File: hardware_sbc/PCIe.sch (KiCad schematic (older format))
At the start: 21 parts, among them J5 Bus_PCI_Express_Mini, U1 IMX8MM

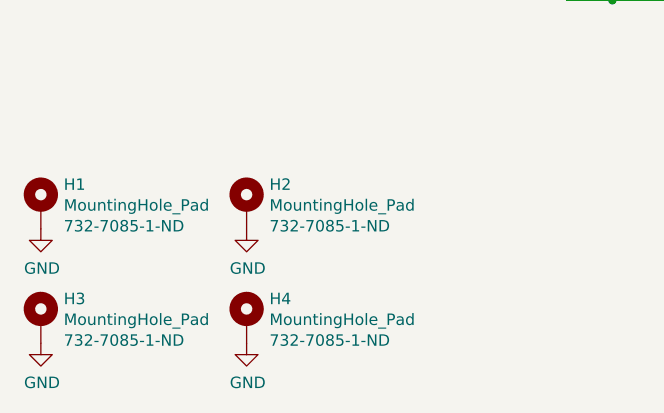
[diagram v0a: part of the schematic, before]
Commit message: BOM and misc fixes for production of 0.9 boards
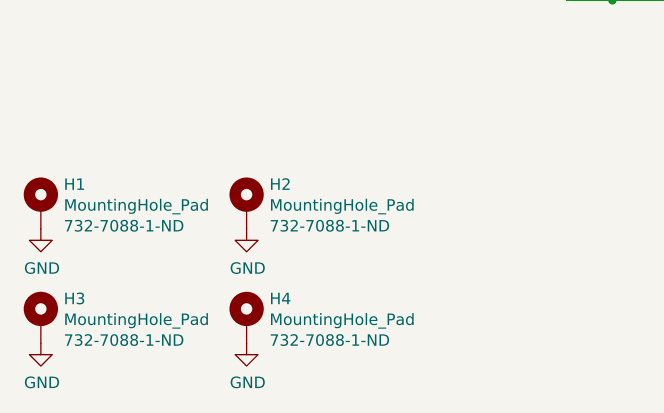
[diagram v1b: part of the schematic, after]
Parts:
- C121, C122, C123: Mfgrpart (none) -> GRM033C80J104KE15D; Part GRM033C80J104KE15D -> (none)
- C124, C130: Mfgrpart (none) -> GRM155C80J475MEAAD; Part GRM155C80J475MEAAD -> (none)
- C125, C126, C127: Mfgrpart (none) -> GRM31CR60J227ME11L; Part GRM31CR60J227ME11L -> (none)
- C128, C129: Mfgrpart (none) -> GRM21BC80G476ME15L; Part GRM21BC80G476ME15L -> (none)
- C131: Mfgrpart (none) -> GRM155C80J106ME11D; Part GRM155C80J106ME11D -> (none)
- D2: Mfgrpart (none) -> MM5Z5V1T1G; Part MM5Z5V1T1G -> (none)
- H1, H2, H3, H4: Mfgrpart (none) -> 9774035243R‎; Part 9774030243R -> (none); Vendorpart 732-7085-1-ND -> 732-7088-1-ND‎
- J5: Mfgrpart (none) -> 1775838-2; Part 1775838-2 -> (none)
- R34, R35: Mfgrpart (none) -> RC0201FR-0749R9L; Part RC0201FR-0749R9L -> (none)
- R36: Mfgrpart (none) -> RC0201FR-078K2L; Part RC0201FR-078K2L -> (none)
- U1: Mfgrpart (none) -> MIMX8MM6CVTKZAA; Part MIMX8MM6CVTKZAA -> (none)
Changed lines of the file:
@@
 F 3 "~" H 7200 2600 50  0001 C CNN
 F 4 "TE" H 7350 3750 50  0001 C CNN "Mfgr"
-F 5 "1775838-2" H 7350 3750 50  0001 C CNN "Part"
+F 5 "" H 7350 3750 50  0001 C CNN "Part"
 F 6 "A123340CT-ND" H 7350 3750 50  0001 C CNN "Vendorpart"
+F 7 "1775838-2" H 7350 3750 50  0001 C CNN "Mfgrpart"
 	1    7350 3750
 	1    0    0    1
@@
 F 3 "" H 2950 8900 50  0001 C CNN
 F 4 "NXP" H 3700 6150 50  0001 C CNN "Mfgr"
-F 5 "MIMX8MM6CVTKZAA" H 3700 6150 50  0001 C CNN "Part"
+F 5 "" H 3700 6150 50  0001 C CNN "Part"
 F 6 "568-15276-ND" H 3700 6150 50  0001 C CNN "Vendorpart"
+F 7 "MIMX8MM6CVTKZAA" H 3700 6150 50  0001 C CNN "Mfgrpart"
 	3    3700 6150
 	1    0    0    -1
@@
 F 3 "~" H 5250 4650 50  0001 C CNN
 F 4 "Yageo" H 5250 4650 50  0001 C CNN "Mfgr"
-F 5 "RC0201FR-078K2L" H 5250 4650 50  0001 C CNN "Part"
+F 5 "" H 5250 4650 50  0001 C CNN "Part"
 F 6 "YAG2353CT-ND" H 5250 4650 50  0001 C CNN "Vendorpart"
+F 7 "RC0201FR-078K2L" H 5250 4650 50  0001 C CNN "Mfgrpart"
 	1    5250 4650
 	1    0    0    -1
@@
 F 3 "~" H 5450 3300 50  0001 C CNN
 F 4 "Yageo" H 5450 3300 50  0001 C CNN "Mfgr"
-F 5 "RC0201FR-0749R9L" H 5450 3300 50  0001 C CNN "Part"
+F 5 "" H 5450 3300 50  0001 C CNN "Part"
 F 6 "YAG2702CT-ND" H 5450 3300 50  0001 C CNN "Vendorpart"
+F 7 "RC0201FR-0749R9L" H 5450 3300 50  0001 C CNN "Mfgrpart"
 	1    5450 3300
 	1    0    0    -1
@@
 F 3 "~" H 5850 3300 50  0001 C CNN
 F 4 "Yageo" H 5850 3300 50  0001 C CNN "Mfgr"
-F 5 "RC0201FR-0749R9L" H 5850 3300 50  0001 C CNN "Part"
+F 5 "" H 5850 3300 50  0001 C CNN "Part"
 F 6 "YAG2702CT-ND" H 5850 3300 50  0001 C CNN "Vendorpart"
+F 7 "RC0201FR-0749R9L" H 5850 3300 50  0001 C CNN "Mfgrpart"
 	1    5850 3300
 	1    0    0    -1
@@
 F 3 "~" H 7900 5350 50  0001 C CNN
 F 4 "Murata" H 7900 5350 50  0001 C CNN "Mfgr"
-F 5 "GRM155C80J475MEAAD" H 7900 5350 50  0001 C CNN "Part"
+F 5 "" H 7900 5350 50  0001 C CNN "Part"
 F 6 "490-14458-1-ND" H 7900 5350 50  0001 C CNN "Vendorpart"
+F 7 "GRM155C80J475MEAAD" H 7900 5350 50  0001 C CNN "Mfgrpart"
 	1    7900 5350
 	1    0    0    -1
@@
 F 3 "~" H 8150 5350 50  0001 C CNN
 F 4 "Murata" H 8150 5350 50  0001 C CNN "Mfgr"
-F 5 "GRM155C80J106ME11D" H 8150 5350 50  0001 C CNN "Part"
+F 5 "" H 8150 5350 50  0001 C CNN "Part"
 F 6 "490-13233-1-ND" H 8150 5350 50  0001 C CNN "Vendorpart"
+F 7 "GRM155C80J106ME11D" H 8150 5350 50  0001 C CNN "Mfgrpart"
 	1    8150 5350
 	1    0    0    -1
@@
 F 3 "~" H 6750 5350 50  0001 C CNN
 F 4 "Murata" H 6750 5350 50  0001 C CNN "Mfgr"
-F 5 "GRM21BC80G476ME15L" H 6750 5350 50  0001 C CNN "Part"
+F 5 "" H 6750 5350 50  0001 C CNN "Part"
 F 6 "490-9954-1-ND" H 6750 5350 50  0001 C CNN "Vendorpart"
+F 7 "GRM21BC80G476ME15L" H 6750 5350 50  0001 C CNN "Mfgrpart"
 	1    6750 5350
 	1    0    0    -1
@@
 F 3 "~" H 6500 5350 50  0001 C CNN
 F 4 "Murata" H 6500 5350 50  0001 C CNN "Mfgr"
-F 5 "GRM21BC80G476ME15L" H 6500 5350 50  0001 C CNN "Part"
+F 5 "" H 6500 5350 50  0001 C CNN "Part"
 F 6 "490-9954-1-ND" H 6500 5350 50  0001 C CNN "Vendorpart"
+F 7 "GRM21BC80G476ME15L" H 6500 5350 50  0001 C CNN "Mfgrpart"
 	1    6500 5350
 	1    0    0    -1
@@
 F 3 "~" H 6250 5350 50  0001 C CNN
 F 4 "Murata" H 6250 5350 50  0001 C CNN "Mfgr"
-F 5 "GRM31CR60J227ME11L" H 6250 5350 50  0001 C CNN "Part"
+F 5 "" H 6250 5350 50  0001 C CNN "Part"
 F 6 "490-13970-1-ND" H 6250 5350 50  0001 C CNN "Vendorpart"
+F 7 "GRM31CR60J227ME11L" H 6250 5350 50  0001 C CNN "Mfgrpart"
 	1    6250 5350
 	1    0    0    -1
@@
 F 3 "~" H 6000 5350 50  0001 C CNN
 F 4 "Murata" H 6000 5350 50  0001 C CNN "Mfgr"
-F 5 "GRM31CR60J227ME11L" H 6000 5350 50  0001 C CNN "Part"
+F 5 "" H 6000 5350 50  0001 C CNN "Part"
 F 6 "490-13970-1-ND" H 6000 5350 50  0001 C CNN "Vendorpart"
+F 7 "GRM31CR60J227ME11L" H 6000 5350 50  0001 C CNN "Mfgrpart"
 	1    6000 5350
 	1    0    0    -1
@@
 F 3 "~" H 5750 5350 50  0001 C CNN
 F 4 "Murata" H 5750 5350 50  0001 C CNN "Mfgr"
-F 5 "GRM31CR60J227ME11L" H 5750 5350 50  0001 C CNN "Part"
+F 5 "" H 5750 5350 50  0001 C CNN "Part"
 F 6 "490-13970-1-ND" H 5750 5350 50  0001 C CNN "Vendorpart"
+F 7 "GRM31CR60J227ME11L" H 5750 5350 50  0001 C CNN "Mfgrpart"
 	1    5750 5350
 	1    0    0    -1
@@
 F 3 "~" H 5500 5350 50  0001 C CNN
 F 4 "Murata" H 5500 5350 50  0001 C CNN "Mfgr"
-F 5 "GRM155C80J475MEAAD" H 5500 5350 50  0001 C CNN "Part"
+F 5 "" H 5500 5350 50  0001 C CNN "Part"
 F 6 "490-14458-1-ND" H 5500 5350 50  0001 C CNN "Vendorpart"
+F 7 "GRM155C80J475MEAAD" H 5500 5350 50  0001 C CNN "Mfgrpart"
 	1    5500 5350
 	1    0    0    -1
@@
 F 3 "~" H 5250 5350 50  0001 C CNN
 F 4 "Murata" H 5250 5350 50  0001 C CNN "Mfgr"
-F 5 "GRM033C80J104KE15D" H 5250 5350 50  0001 C CNN "Part"
+F 5 "" H 5250 5350 50  0001 C CNN "Part"
 F 6 "490-10390-1-ND" H 5250 5350 50  0001 C CNN "Vendorpart"
+F 7 "GRM033C80J104KE15D" H 5250 5350 50  0001 C CNN "Mfgrpart"
 	1    5250 5350
 	1    0    0    -1
@@
 F 3 "~" H 5500 4250 50  0001 C CNN
 F 4 "Murata" H 5500 4250 50  0001 C CNN "Mfgr"
-F 5 "GRM033C80J104KE15D" H 5500 4250 50  0001 C CNN "Part"
+F 5 "" H 5500 4250 50  0001 C CNN "Part"
 F 6 "490-10390-1-ND" H 5500 4250 50  0001 C CNN "Vendorpart"
+F 7 "GRM033C80J104KE15D" H 5500 4250 50  0001 C CNN "Mfgrpart"
 	1    5500 4250
 	0    1    1    0
@@
 F 3 "~" H 5400 4150 50  0001 C CNN
 F 4 "Murata" H 5400 4150 50  0001 C CNN "Mfgr"
-F 5 "GRM033C80J104KE15D" H 5400 4150 50  0001 C CNN "Part"
+F 5 "" H 5400 4150 50  0001 C CNN "Part"
 F 6 "490-10390-1-ND" H 5400 4150 50  0001 C CNN "Vendorpart"
+F 7 "GRM033C80J104KE15D" H 5400 4150 50  0001 C CNN "Mfgrpart"
 	1    5400 4150
 	0    1    1    0
@@
 F 4 "MM5Z5V1T1GOSCT-ND" V 5141 5271 50  0000 R CNN "Vendorpart"
 F 5 "On Semi" H 5050 5350 50  0001 C CNN "Mfgr"
-F 6 "MM5Z5V1T1G" H 5050 5350 50  0001 C CNN "Part"
+F 6 "" H 5050 5350 50  0001 C CNN "Part"
+F 7 "MM5Z5V1T1G" H 5050 5350 50  0001 C CNN "Mfgrpart"
 	1    5050 5350
 	0    1    1    0
@@
 F 2 "mxenc:MountingHole_M2_Standoff" H 2750 6400 50  0001 C CNN
 F 3 "~" H 2750 6400 50  0001 C CNN
-F 4 "732-7085-1-ND" H 2850 6312 50  0000 L CNN "Vendorpart"
+F 4 "732-7088-1-ND‎" H 2850 6312 50  0000 L CNN "Vendorpart"
 F 5 "Wurth" H 2750 6400 50  0001 C CNN "Mfgr"
-F 6 "9774030243R" H 2750 6400 50  0001 C CNN "Part"
+F 6 "" H 2750 6400 50  0001 C CNN "Part"
+F 7 "9774035243R‎" H 2750 6400 50  0001 C CNN "Mfgrpart"
 	1    2750 6400
 	1    0    0    -1
@@
 F 2 "mxenc:MountingHole_M2_Standoff" H 3650 6400 50  0001 C CNN
 F 3 "~" H 3650 6400 50  0001 C CNN
-F 4 "732-7085-1-ND" H 3750 6312 50  0000 L CNN "Vendorpart"
+F 4 "732-7088-1-ND‎" H 3750 6312 50  0000 L CNN "Vendorpart"
 F 5 "Wurth" H 3650 6400 50  0001 C CNN "Mfgr"
-F 6 "9774030243R" H 3650 6400 50  0001 C CNN "Part"
+F 6 "" H 3650 6400 50  0001 C CNN "Part"
+F 7 "9774035243R‎" H 3650 6400 50  0001 C CNN "Mfgrpart"
 	1    3650 6400
 	1    0    0    -1
@@
 F 2 "mxenc:MountingHole_M2_Standoff" H 3650 6900 50  0001 C CNN
 F 3 "~" H 3650 6900 50  0001 C CNN
-F 4 "732-7085-1-ND" H 3750 6812 50  0000 L CNN "Vendorpart"
+F 4 "732-7088-1-ND‎" H 3750 6812 50  0000 L CNN "Vendorpart"
 F 5 "Wurth" H 3650 6900 50  0001 C CNN "Mfgr"
-F 6 "9774030243R" H 3650 6900 50  0001 C CNN "Part"
+F 6 "" H 3650 6900 50  0001 C CNN "Part"
+F 7 "9774035243R‎" H 3650 6900 50  0001 C CNN "Mfgrpart"
 	1    3650 6900
 	1    0    0    -1
@@
 F 2 "mxenc:MountingHole_M2_Standoff" H 2750 6900 50  0001 C CNN
 F 3 "~" H 2750 6900 50  0001 C CNN
-F 4 "732-7085-1-ND" H 2850 6812 50  0000 L CNN "Vendorpart"
+F 4 "732-7088-1-ND‎" H 2850 6812 50  0000 L CNN "Vendorpart"
 F 5 "Wurth" H 2750 6900 50  0001 C CNN "Mfgr"
-F 6 "9774030243R" H 2750 6900 50  0001 C CNN "Part"
+F 6 "" H 2750 6900 50  0001 C CNN "Part"
+F 7 "9774035243R‎" H 2750 6900 50  0001 C CNN "Mfgrpart"
 	1    2750 6900
 	1    0    0    -1

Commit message: Don't stuff C125-127
These 3x 220uF caps are pulling down the 3v3 at boot. We need a
load switch in the next rev.
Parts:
- C125, C126, C127: Populate (none) -> DNP
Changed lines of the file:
@@
 F 6 "490-13970-1-ND" H 6250 5350 50  0001 C CNN "Vendorpart"
 F 7 "GRM31CR60J227ME11L" H 6250 5350 50  0001 C CNN "Mfgrpart"
+F 8 "DNP" H 6250 5350 50  0000 C CNN "Populate"
 	1    6250 5350
 	1    0    0    -1
@@
 F 6 "490-13970-1-ND" H 6000 5350 50  0001 C CNN "Vendorpart"
 F 7 "GRM31CR60J227ME11L" H 6000 5350 50  0001 C CNN "Mfgrpart"
+F 8 "DNP" H 6000 5350 50  0000 C CNN "Populate"
 	1    6000 5350
 	1    0    0    -1
@@
 F 6 "490-13970-1-ND" H 5750 5350 50  0001 C CNN "Vendorpart"
 F 7 "GRM31CR60J227ME11L" H 5750 5350 50  0001 C CNN "Mfgrpart"
+F 8 "DNP" H 5750 5350 50  0000 C CNN "Populate"
 	1    5750 5350
 	1    0    0    -1

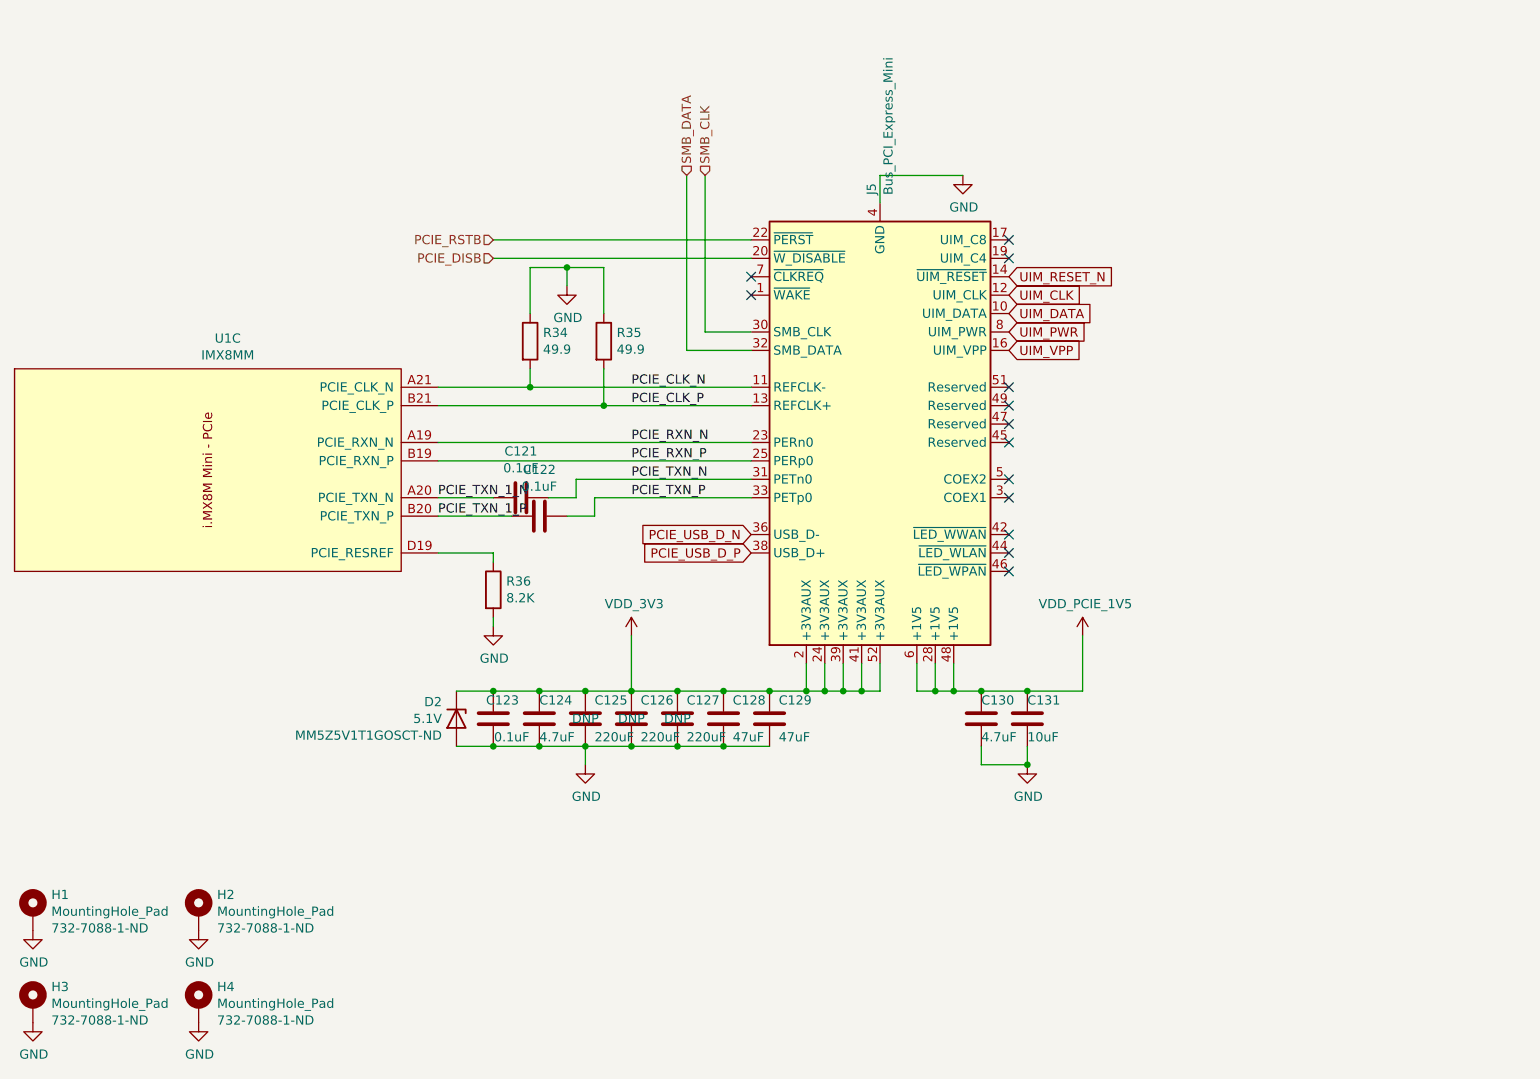
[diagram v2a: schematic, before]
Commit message: Update BoM and add some errata notes for v0.9 builds moving forward
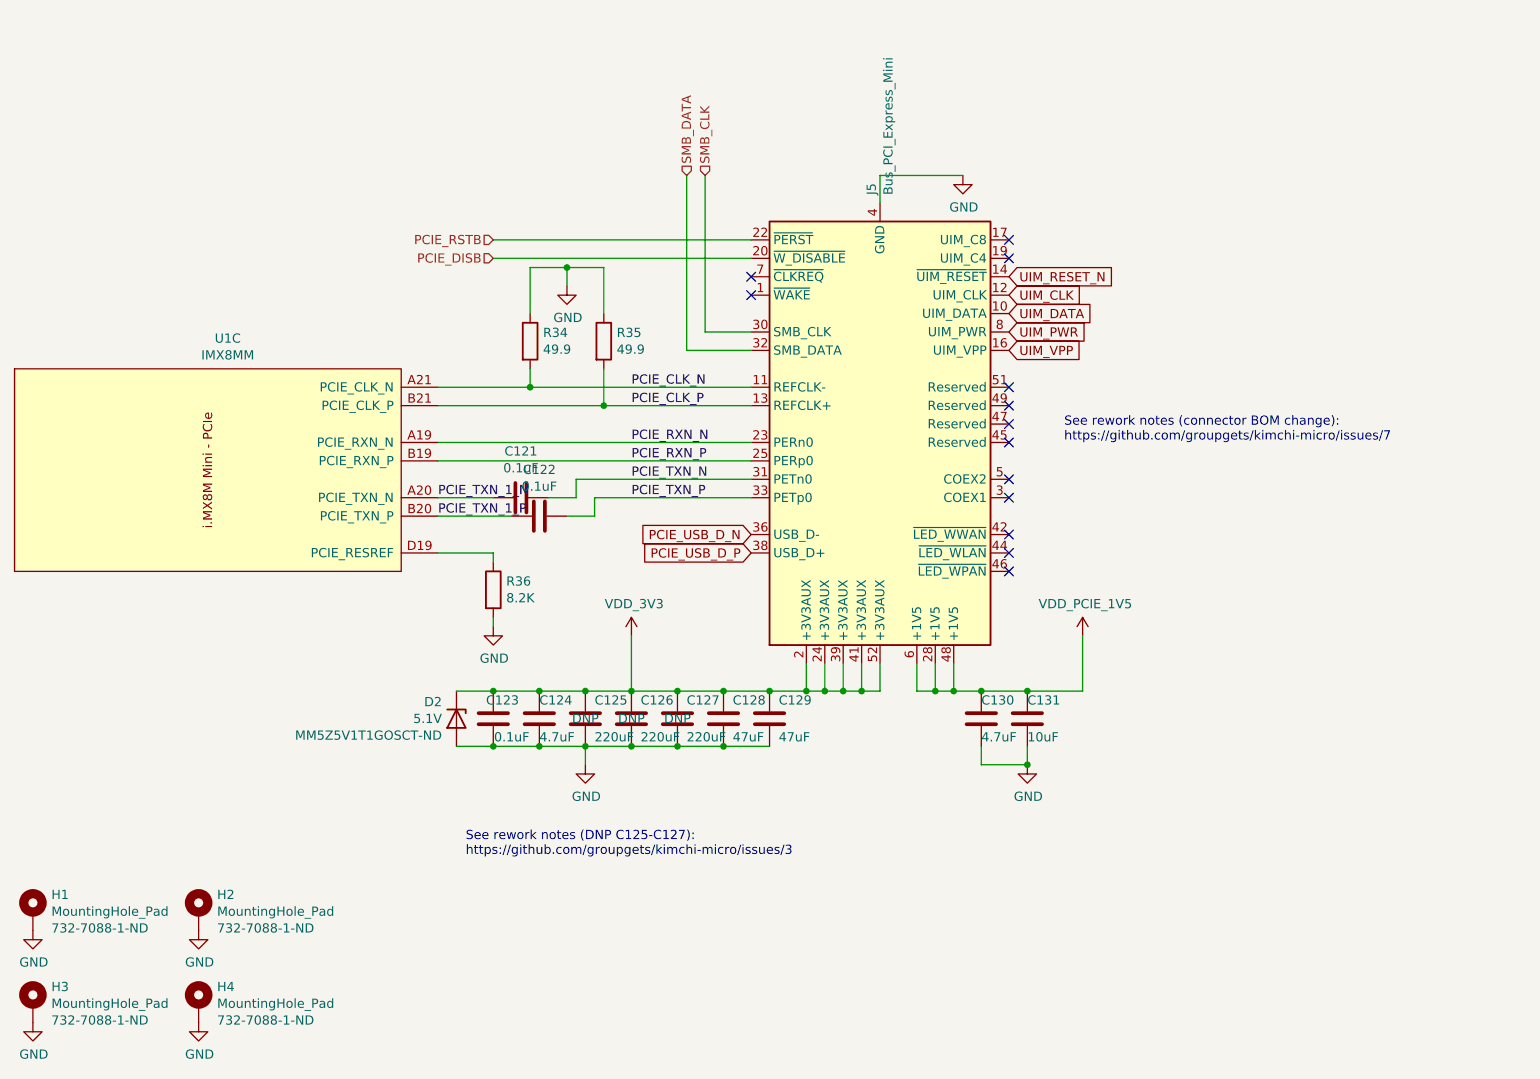
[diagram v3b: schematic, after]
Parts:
- J5: Mfgrpart 1775838-2 -> 2041262-1; Vendorpart A123340CT-ND -> A125147CT-ND
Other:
- note added: "See rework notes (DNP C125-C127):\nhttps://github.com/groupgets/kimchi-micro/issues/3"
- note added: "See rework notes (connector BOM change):\nhttps://github.com/groupgets/kimchi-micro/issues/7"
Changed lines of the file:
@@
 F 4 "TE" H 7350 3750 50  0001 C CNN "Mfgr"
 F 5 "" H 7350 3750 50  0001 C CNN "Part"
-F 6 "A123340CT-ND" H 7350 3750 50  0001 C CNN "Vendorpart"
-F 7 "1775838-2" H 7350 3750 50  0001 C CNN "Mfgrpart"
+F 6 "A125147CT-ND" H 7350 3750 50  0001 C CNN "Vendorpart"
+F 7 "2041262-1" H 7350 3750 50  0001 C CNN "Mfgrpart"
 	1    7350 3750
 	1    0    0    1
@@
 	1    0    0    -1
 $EndComp
+Text Notes 5100 6100 0    50   ~ 0
+See rework notes (DNP C125-C127):\nhttps://github.com/groupgets/kimchi-micro/issues/3
+Text Notes 8350 3850 0    50   ~ 0
+See rework notes (connector BOM change):\nhttps://github.com/groupgets/kimchi-micro/issues/7
 $EndSCHEMATC
